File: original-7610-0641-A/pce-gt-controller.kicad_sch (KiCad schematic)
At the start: 30 parts, among them CN800 Conn_01x12, CN801 AUDIO, IC800 BU5782K, J800 LINK, SW801 I, SW802 II, SW803 SELECT, SW804 RUN, SW805 UP, SW806 RIGHT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

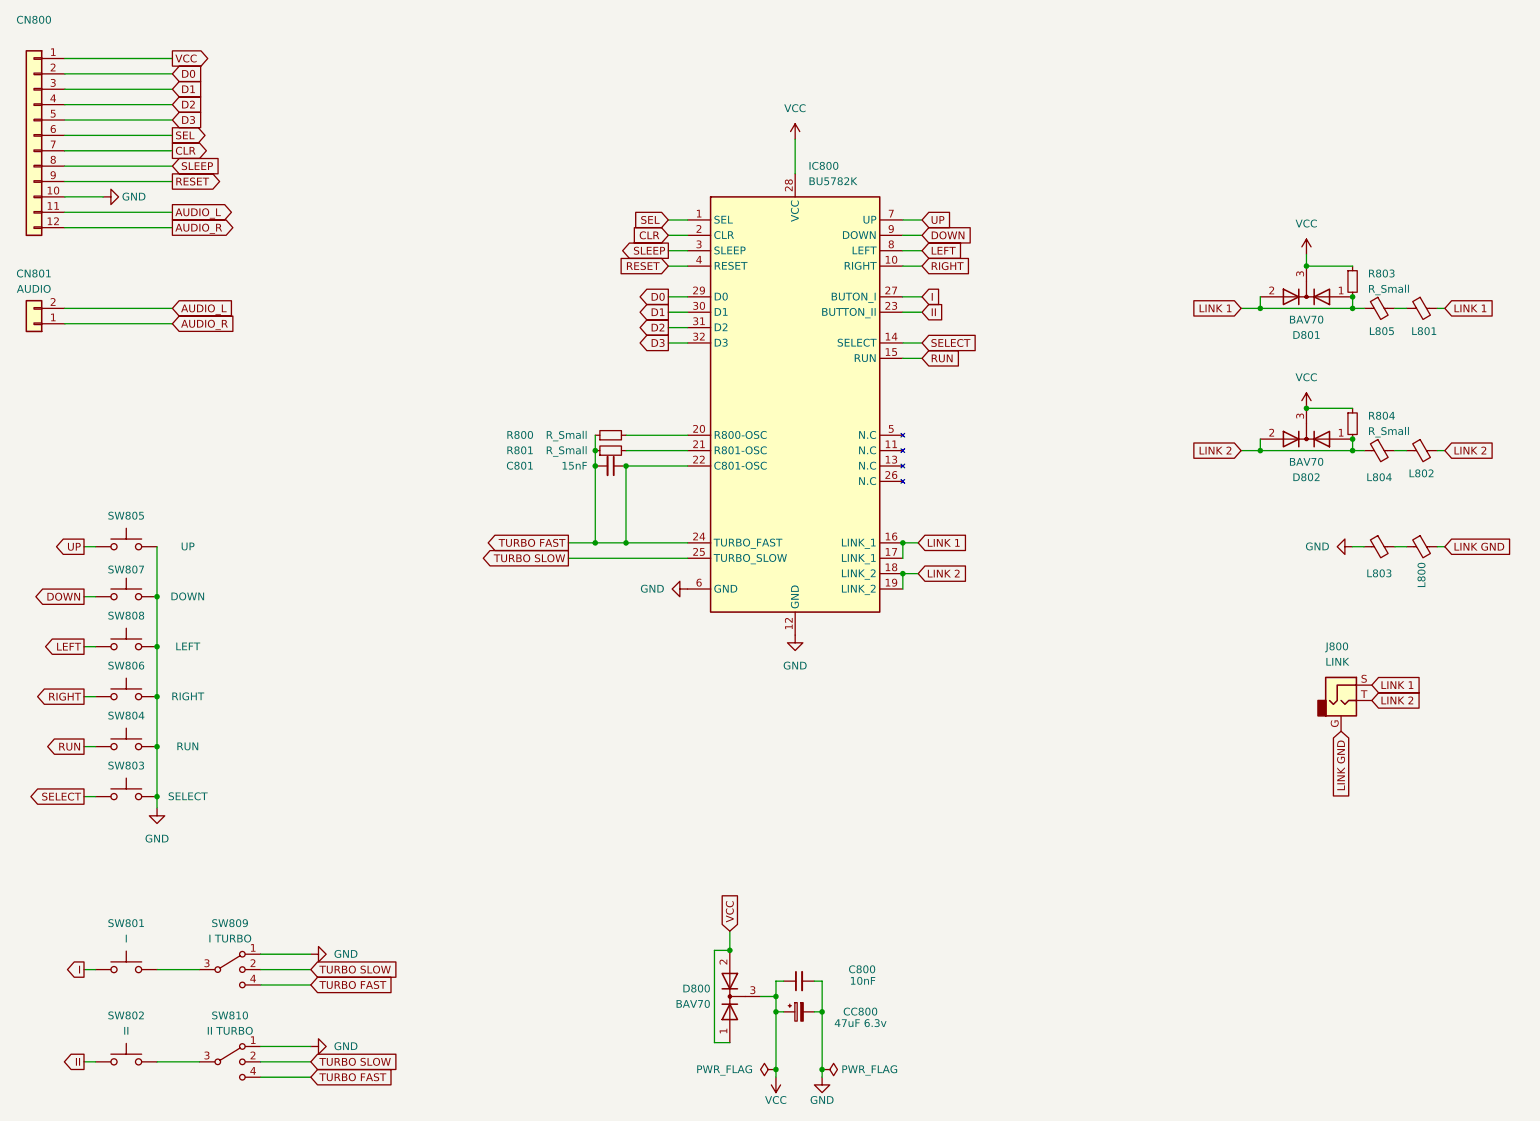
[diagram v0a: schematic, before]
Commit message: Update to original, fix slight mistake linking fast turbo
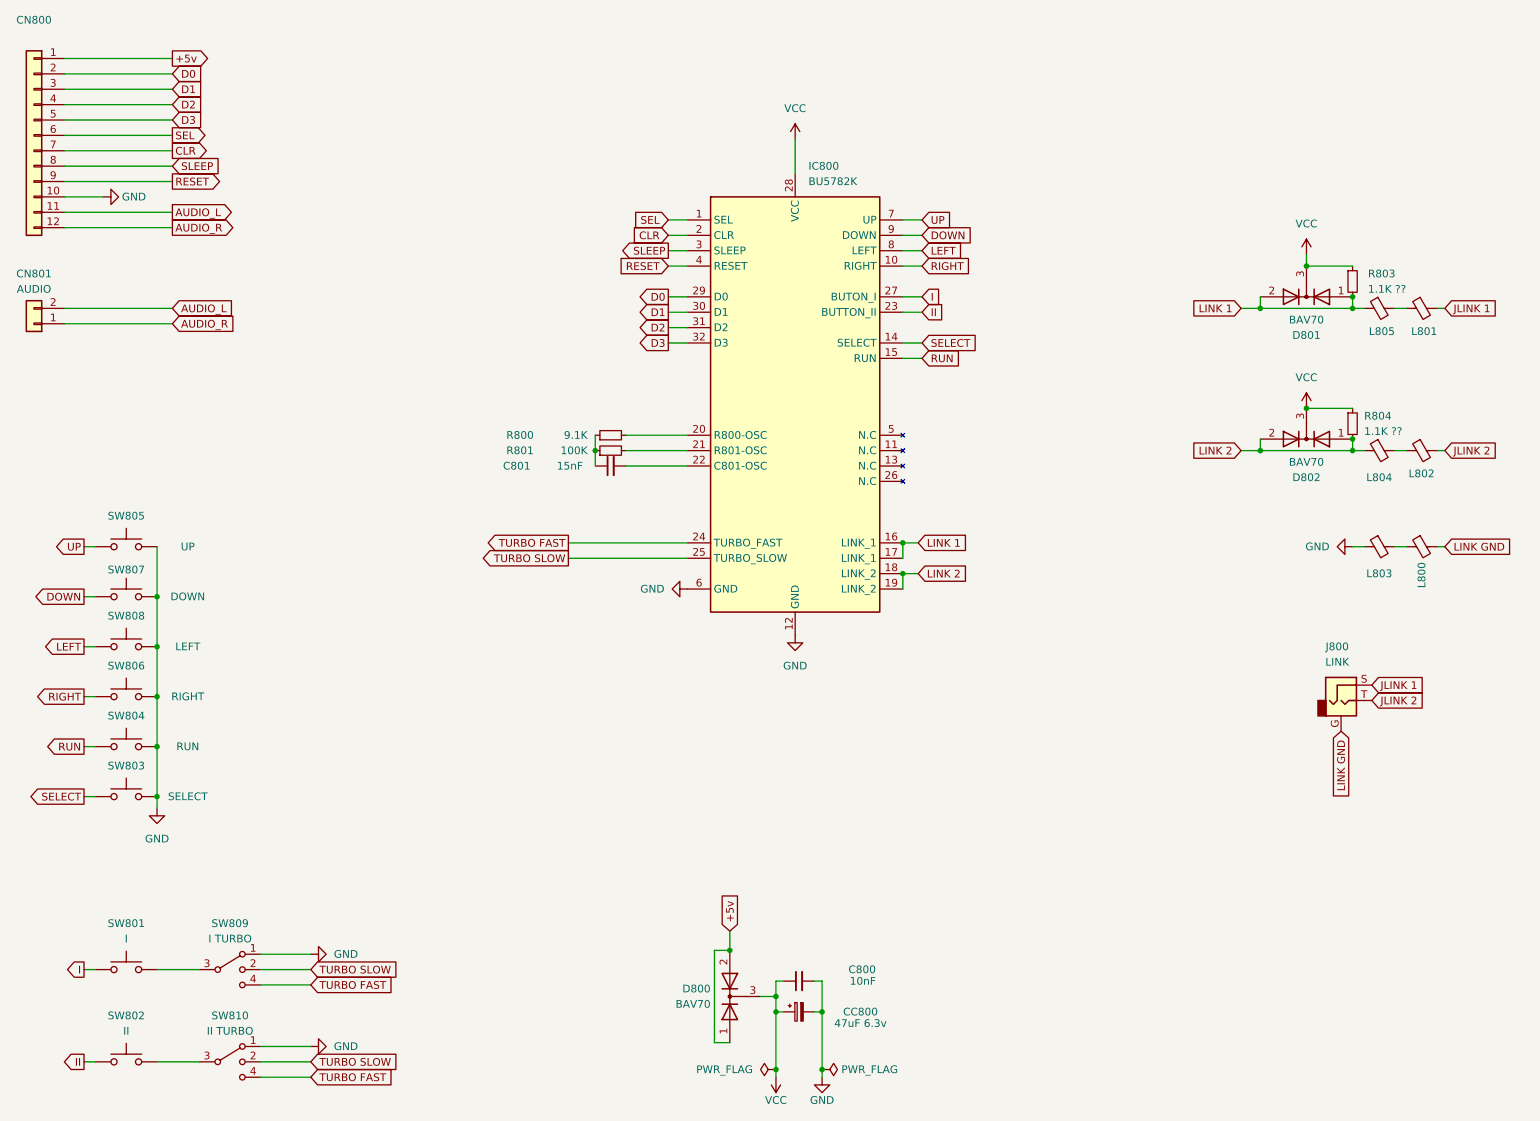
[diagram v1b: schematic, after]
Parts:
- R800: value R_Small -> 9.1K
- R801: value R_Small -> 100K
- R803, R804: value R_Small -> 1.1K ??
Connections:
- net LINK 1: no longer J800.S, L801.2
- net LINK 2: no longer J800.T, L802.2
- net TURBO FAST: no longer C801.1, C801.2, IC800.22 (C801-OSC), R800.1, R801.1
- net VCC: no longer CN800.1 (Pin_1), D800.1 (A), D800.2 (A)
- new net: C801.2, IC800.22 (C801-OSC)
- new net: C801.1, R800.1, R801.1
- new net +5v: CN800.1 (Pin_1), D800.1 (A), D800.2 (A)
- new net JLINK 1: J800.S, L801.2
- new net JLINK 2: J800.T, L802.2
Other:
- moved on the sheet: C801
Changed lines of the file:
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@@
   (junction (at 40.64 109.22) (diameter 0) (color 0 0 0 0)
   )
-  (junction (at 118.11 100.33) (diameter 0) (color 0 0 0 0)
-  )
   (junction (at 150.495 187.325) (diameter 0) (color 0 0 0 0)
   )
@@
   (junction (at 135.255 167.64) (diameter 0) (color 0 0 0 0)
   )
-  (junction (at 113.03 87.63) (diameter 0) (color 0 0 0 0)
-  )
   (junction (at 142.875 175.26) (diameter 0) (color 0 0 0 0)
   )
-  (junction (at 113.03 100.33) (diameter 0) (color 0 0 0 0)
-  )
   (junction (at 222.885 61.595) (diameter 0) (color 0 0 0 0)
   )
-  (junction (at 118.11 87.63) (diameter 0) (color 0 0 0 0)
-  )
   (junction (at 40.64 125.73) (diameter 0) (color 0 0 0 0)
   )
@@
     (stroke (width 0) (type default))
   )
-  (wire (pts (xy 118.11 100.33) (xy 118.11 87.63))
-    (stroke (width 0) (type default))
-  )
   (wire (pts (xy 167.005 54.61) (xy 163.83 54.61))
     (stroke (width 0) (type default))
@@
     (stroke (width 0) (type default))
   )
-  (wire (pts (xy 113.03 87.63) (xy 113.03 100.33))
-    (stroke (width 0) (type default))
-  )
   (wire (pts (xy 140.335 175.26) (xy 142.875 175.26))
     (stroke (width 0) (type default))
   )
-  (wire (pts (xy 113.03 100.33) (xy 118.11 100.33))
-    (stroke (width 0) (type default))
-  )
   (wire (pts (xy 125.095 62.23) (xy 128.27 62.23))
     (stroke (width 0) (type default))
@@
     (stroke (width 0) (type default))
   )
-  (wire (pts (xy 128.27 100.33) (xy 118.11 100.33))
-    (stroke (width 0) (type default))
-  )
   (wire (pts (xy 167.005 69.85) (xy 163.83 69.85))
     (stroke (width 0) (type default))
@@
     (stroke (width 0) (type default))
   )
-  (wire (pts (xy 108.585 100.33) (xy 113.03 100.33))
+  (wire (pts (xy 108.585 100.33) (xy 128.27 100.33))
     (stroke (width 0) (type default))
   )
@@
     (stroke (width 0) (type default))
   )
-  (global_label "LINK 2" (shape input) (at 241.3 126.365 0) (fields_autoplaced)
-    (effects (font (size 1.27 1.27)) (justify left))
-    (property "Intersheetrefs" "${INTERSHEET_REFS}" (at 250.6957 126.365 0)
+  (global_label "JLINK 2" (shape input) (at 241.3 126.365 0) (fields_autoplaced)
+    (effects (font (size 1.27 1.27)) (justify left))
+    (property "Intersheetrefs" "${INTERSHEET_REFS}" (at 251.6633 126.365 0)
       (effects (font (size 1.27 1.27)) (justify left) hide)
     )
@@
     )
   )
-  (global_label "LINK 1" (shape input) (at 253.365 61.595 0) (fields_autoplaced)
-    (effects (font (size 1.27 1.27)) (justify left))
-    (property "Intersheetrefs" "${INTERSHEET_REFS}" (at 262.7607 61.595 0)
+  (global_label "JLINK 1" (shape input) (at 253.365 61.595 0) (fields_autoplaced)
+    (effects (font (size 1.27 1.27)) (justify left))
+    (property "Intersheetrefs" "${INTERSHEET_REFS}" (at 263.7283 61.595 0)
       (effects (font (size 1.27 1.27)) (justify left) hide)
     )
@@
     )
   )
-  (global_label "VCC" (shape output) (at 43.18 20.32 0) (fields_autoplaced)
-    (effects (font (size 1.27 1.27)) (justify left))
-    (property "Intersheetrefs" "${INTERSHEET_REFS}" (at 49.7938 20.32 0)
+  (global_label "+5v" (shape output) (at 43.18 20.32 0) (fields_autoplaced)
+    (effects (font (size 1.27 1.27)) (justify left))
+    (property "Intersheetrefs" "${INTERSHEET_REFS}" (at 49.9147 20.32 0)
       (effects (font (size 1.27 1.27)) (justify left) hide)
     )
@@
     )
   )
-  (global_label "LINK 2" (shape input) (at 253.365 85.09 0) (fields_autoplaced)
-    (effects (font (size 1.27 1.27)) (justify left))
-    (property "Intersheetrefs" "${INTERSHEET_REFS}" (at 262.7607 85.09 0)
-      (effects (font (size 1.27 1.27)) (justify left) hide)
-    )
-  )
-  (global_label "LINK 1" (shape input) (at 241.3 123.825 0) (fields_autoplaced)
-    (effects (font (size 1.27 1.27)) (justify left))
-    (property "Intersheetrefs" "${INTERSHEET_REFS}" (at 250.6957 123.825 0)
+  (global_label "JLINK 2" (shape input) (at 253.365 85.09 0) (fields_autoplaced)
+    (effects (font (size 1.27 1.27)) (justify left))
+    (property "Intersheetrefs" "${INTERSHEET_REFS}" (at 263.7283 85.09 0)
+      (effects (font (size 1.27 1.27)) (justify left) hide)
+    )
+  )
+  (global_label "JLINK 1" (shape input) (at 241.3 123.825 0) (fields_autoplaced)
+    (effects (font (size 1.27 1.27)) (justify left))
+    (property "Intersheetrefs" "${INTERSHEET_REFS}" (at 251.6633 123.825 0)
       (effects (font (size 1.27 1.27)) (justify left) hide)
     )
@@
     )
   )
-  (global_label "VCC" (shape input) (at 135.255 164.465 90) (fields_autoplaced)
-    (effects (font (size 1.27 1.27)) (justify left))
-    (property "Intersheetrefs" "${INTERSHEET_REFS}" (at 135.255 157.8512 90)
+  (global_label "+5v" (shape input) (at 135.255 164.465 90) (fields_autoplaced)
+    (effects (font (size 1.27 1.27)) (justify left))
+    (property "Intersheetrefs" "${INTERSHEET_REFS}" (at 135.255 157.7303 90)
       (effects (font (size 1.27 1.27)) (justify left) hide)
     )
@@
   (symbol (lib_id "Device:R_Small") (at 238.125 80.645 0) (unit 1)
     (in_bom yes) (on_board yes) (dnp no) (fields_autoplaced)
-    (property "Reference" "R804" (at 240.665 79.375 0)
-      (effects (font (size 1.27 1.27)) (justify left))
-    )
-    (property "Value" "R_Small" (at 240.665 81.915 0)
+    (property "Reference" "R804" (at 240.03 79.375 0)
+      (effects (font (size 1.27 1.27)) (justify left))
+    )
+    (property "Value" "1.1K ??" (at 240.03 81.915 0)
       (effects (font (size 1.27 1.27)) (justify left))
     )
@@
       (effects (font (size 1.27 1.27)) (justify left))
     )
-    (property "Value" "R_Small" (at 111.76 82.55 90)
+    (property "Value" "9.1K" (at 111.76 82.55 90)
       (effects (font (size 1.27 1.27)) (justify left))
     )
@@
     )
   )
-  (symbol (lib_id "Device:C_Small") (at 115.57 87.63 270) (unit 1)
-    (in_bom yes) (on_board yes) (dnp no)
-    (property "Reference" "C801" (at 102.87 87.63 90)
+  (symbol (lib_id "Device:C_Small") (at 115.57 87.63 90) (unit 1)
+    (in_bom yes) (on_board yes) (dnp no)
+    (property "Reference" "C801" (at 97.79 87.63 90)
       (effects (font (size 1.27 1.27)) (justify right))
     )
-    (property "Value" "15nF" (at 111.76 87.63 90)
+    (property "Value" "15nF" (at 106.68 87.63 90)
       (effects (font (size 1.27 1.27)) (justify right))
     )
@@
       (effects (font (size 1.27 1.27)) (justify left))
     )
-    (property "Value" "R_Small" (at 240.665 58.42 0)
+    (property "Value" "1.1K ??" (at 240.665 58.42 0)
       (effects (font (size 1.27 1.27)) (justify left))
     )
@@
       (effects (font (size 1.27 1.27)) (justify left))
     )
-    (property "Value" "R_Small" (at 111.76 85.09 90)
-      (effects (font (size 1.27 1.27)) (justify left))
-    )
+    (property "Value" "100K" (at 111.76 85.09 90)
+      (effects (font (size 1.27 1.27)) (justify left))
+    )

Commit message: Added BoardFolk Silk, Tidy up
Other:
- title: PC Engine GT Controller PCB -> PC Engine GT Controller PCB (Original)
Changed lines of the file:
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@@
   (paper "A4")
   (title_block
-    (title "PC Engine GT Controller PCB")
-    (date "2023-11-06")
-    (rev "1.0")
+    (title "PC Engine GT Controller PCB (Original)")
+    (date "2023-12-31")
+    (rev "1.1")
     (company "The Board Folk Team")
   )
